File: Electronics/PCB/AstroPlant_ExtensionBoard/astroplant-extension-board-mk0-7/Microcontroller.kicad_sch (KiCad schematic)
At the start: 40 parts, among them J12 CONUFL001-SMD-T, J6 629105136821, SW3 SW_Push, U1 USBLC6-2SC6, U2 STM32WB55RGVx

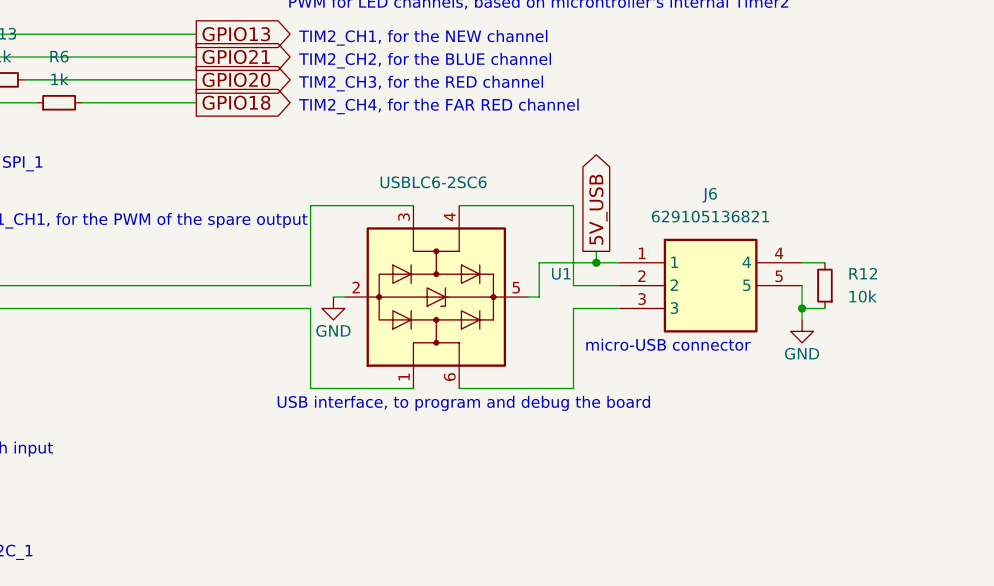
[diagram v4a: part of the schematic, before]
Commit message: Solved processing notes from aisler by changing micro usb connector
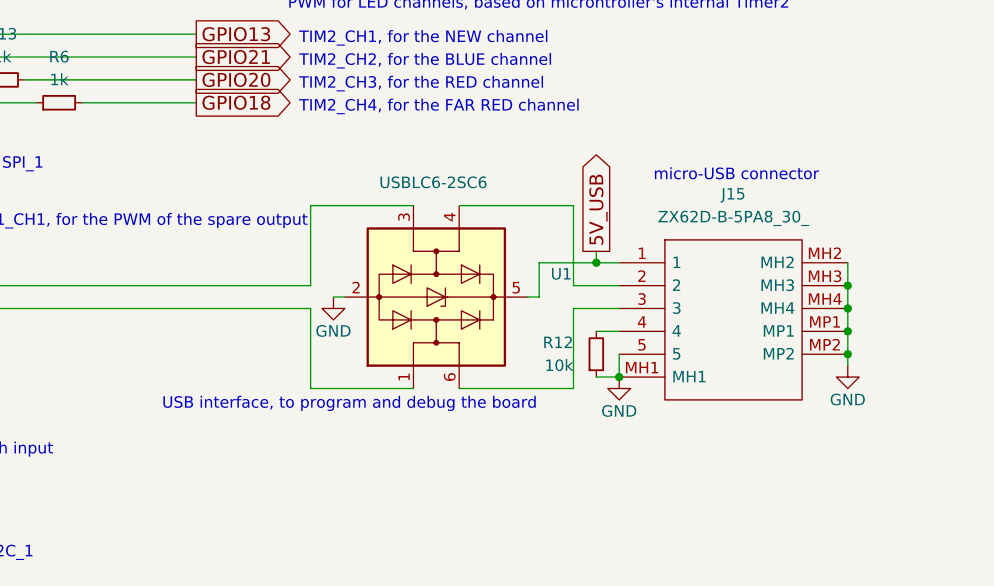
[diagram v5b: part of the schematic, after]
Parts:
- removed J6: 629105136821, SamacSys_Parts:MICRO-USB_2.0-SMT-TYPE-B_, symbol SamacSys_Parts:629105136821
- added J15: ZX62D-B-5PA8_30_, ZX62DB5PA830, symbol SamacSys_Parts:ZX62D-B-5PA8_30_
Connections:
- net 5V_USB: now also J15.1
- net GND: now also J15.5, J15.MH1, J15.MH2, J15.MH3, J15.MH4, J15.MP1, J15.MP2
- net at U1.4 (I/O2): now also J15.2
- net at U1.6 (I/O1): now also J15.3
- net at R12.2: now also J15.4
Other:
- moved on the sheet: R12

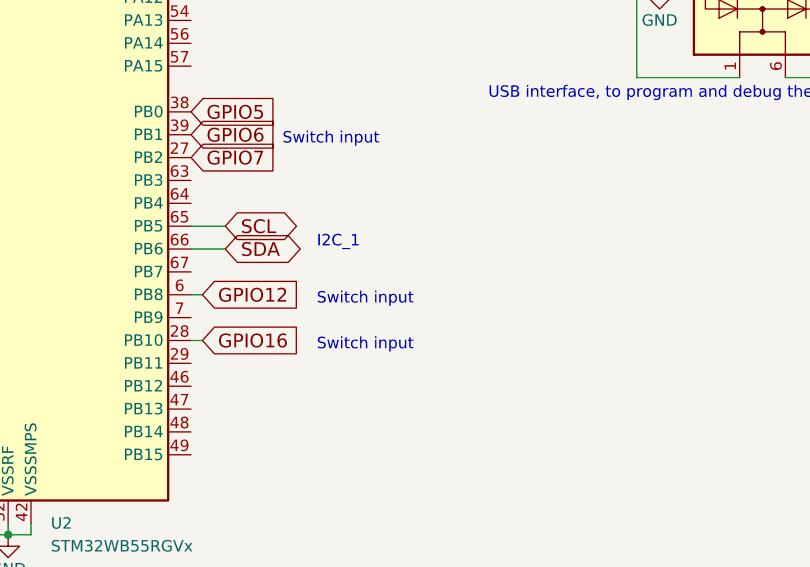
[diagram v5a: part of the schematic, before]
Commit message: Changed PCB, add a LED to simplify tests
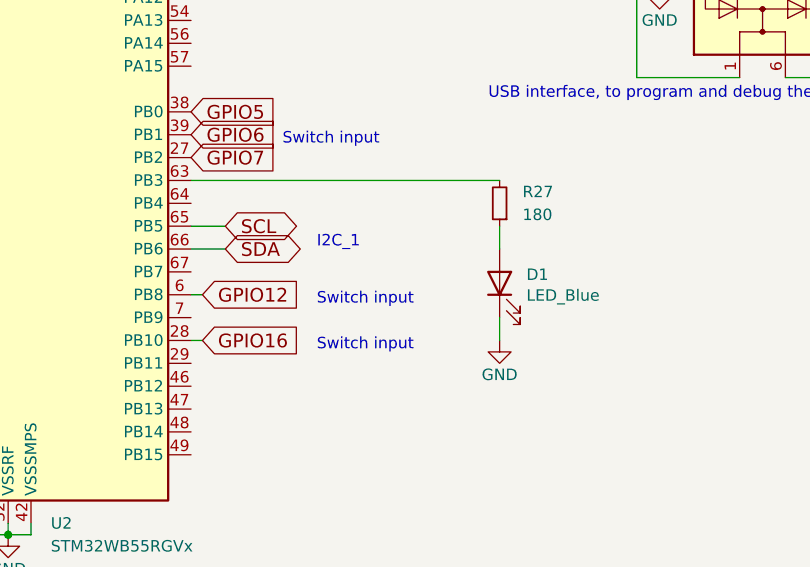
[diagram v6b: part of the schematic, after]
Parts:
- added D1: LED_Blue, LED_SMD:LED_0603_1608Metric, symbol Device:LED
- added R27: 180, Resistor_SMD:R_0603_1608Metric, symbol Device:R_Small
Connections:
- net GND: now also D1.1 (K)
- net at U2.63 (PB3): now also R27.2
- new net: D1.2 (A), R27.1
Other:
- title: (none) -> Microcontroller
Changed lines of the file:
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@@
 (kicad_sch (version 20230121) (generator eeschema)
   (paper "A4")
+  (title_block
+    (title "Microcontroller")
+    (date "2023-10-13")
+    (rev "0.7")
+    (comment 1 "Aurélien Lesage")
+  )
   (junction (at 106.68 25.4) (diameter 0) (color 0 0 0 0)
   )
@@
     (stroke (width 0) (type default))
   )
+  (wire (pts (xy 207.01 106.68) (xy 207.01 109.22))
+    (stroke (width 0) (type default))
+  )
   (wire (pts (xy 127 25.4) (xy 137.16 25.4))
     (stroke (width 0) (type default))
@@
     (stroke (width 0) (type default))
   )
+  (wire (pts (xy 172.72 101.6) (xy 207.01 101.6))
+    (stroke (width 0) (type default))
+  )
   (wire (pts (xy 105.41 124.46) (xy 113.03 124.46))
     (stroke (width 0) (type default))
@@
   )
   (wire (pts (xy 190.5 55.88) (xy 209.55 55.88))
+    (stroke (width 0) (type default))
+  )
+  (wire (pts (xy 207.01 119.38) (xy 207.01 116.84))
     (stroke (width 0) (type default))
   )
@@
     )
   )
+  (symbol (lib_id "Device:LED") (at 207.01 113.03 90) (unit 1)
+    (in_bom yes) (on_board yes) (dnp no)
+    (property "Reference" "D1" (at 209.9818 112.0648 90)
+      (effects (font (size 1.27 1.27)) (justify right))
+    )
+    (property "Value" "LED_Blue" (at 209.9818 114.3762 90)
+      (effects (font (size 1.27 1.27)) (justify right))
+    )
+    (property "Footprint" "LED_SMD:LED_0603_1608Metric" (at 207.01 113.03 0)
+      (effects (font (size 1.27 1.27)) hide)
+    )
+    (property "Datasheet" "https://fscdn.rohm.com/en/products/databook/datasheet/opto/led/chip_mono/smlen3bc8tt86-e.pdf" (at 207.01 113.03 0)
+      (effects (font (size 1.27 1.27)) hide)
+    )
+    (property "MPN" "SMLEN3BC8TT86" (at 207.01 113.03 0)
+      (effects (font (size 1.27 1.27)) hide)
+    )
+    (property "Mouser PN" " 755-SMLEN3BC8TT86 " (at 207.01 113.03 0)
+      (effects (font (size 1.27 1.27)) hide)
+    )
+    (pin "1")
+    (pin "2")
+    (instances
+      (project "Astroplant_VFR"
+        (path "/4e818498-015c-45b7-982b-80c19490efdc"
+          (reference "D1") (unit 1)
+        )
+      )
+      (project "Astroplant_AL"
+        (path "/51acab52-3cd6-4bba-9dee-c12efd332038"
+          (reference "D6") (unit 1)
+        )
+        (path "/51acab52-3cd6-4bba-9dee-c12efd332038/5f0c961f-7fa6-4a15-8a74-755a432cc19e"
+          (reference "D6") (unit 1)
+        )
+      )
+    )
+  )
   (symbol (lib_id "Device:C_Small") (at 127 27.94 0) (unit 1)
     (in_bom yes) (on_board yes) (dnp no) (fields_autoplaced)
@@
         (path "/51acab52-3cd6-4bba-9dee-c12efd332038/5f0c961f-7fa6-4a15-8a74-755a432cc19e"
           (reference "#PWR020") (unit 1)
+        )
+      )
+    )
+  )
+  (symbol (lib_id "Device:R_Small") (at 207.01 104.14 180) (unit 1)
+    (in_bom yes) (on_board yes) (dnp no) (fields_autoplaced)
+    (property "Reference" "R27" (at 209.55 102.87 0)
+      (effects (font (size 1.27 1.27)) (justify right))
+    )
+    (property "Value" "180" (at 209.55 105.41 0)
+      (effects (font (size 1.27 1.27)) (justify right))
+    )
+    (property "Footprint" "Resistor_SMD:R_0603_1608Metric" (at 207.01 104.14 0)
+      (effects (font (size 1.27 1.27)) hide)
+    )
+    (property "Datasheet" "~" (at 207.01 104.14 0)
+      (effects (font (size 1.27 1.27)) hide)
+    )
+    (property "MPN" "CRCW0603180RFKEA" (at 207.01 104.14 0)
+      (effects (font (size 1.27 1.27)) hide)
+    )
+    (pin "1")
+    (pin "2")
+    (instances
+      (project "Astroplant_AL"
+        (path "/51acab52-3cd6-4bba-9dee-c12efd332038/5f0c961f-7fa6-4a15-8a74-755a432cc19e"
+          (reference "R27") (unit 1)
+        )
+        (path "/51acab52-3cd6-4bba-9dee-c12efd332038/00000000-0000-0000-0000-00005a8053d4"
+          (reference "R11") (unit 1)
+        )
+        (path "/51acab52-3cd6-4bba-9dee-c12efd332038"
+          (reference "R27") (unit 1)
         )
       )
@@
         )
       )
+    )
+  )
+  (symbol (lib_id "power:GND") (at 207.01 119.38 0) (unit 1)
+    (in_bom yes) (on_board yes) (dnp no)
+    (property "Reference" "#PWR0127" (at 207.01 125.73 0)
+      (effects (font (size 1.27 1.27)) hide)
+    )
+    (property "Value" "GND" (at 207.01 123.19 0)
+      (effects (font (size 1.27 1.27)))
+    )
+    (property "Footprint" "" (at 207.01 119.38 0)
+      (effects (font (size 1.27 1.27)) hide)
+    )
+    (property "Datasheet" "" (at 207.01 119.38 0)
+      (effects (font (size 1.27 1.27)) hide)
+    )
+    (pin "1")
+    (instances
+      (project "Astroplant_VFR"
+        (path "/4e818498-015c-45b7-982b-80c19490efdc"
+          (reference "#PWR0127") (unit 1)
+        )
+      )
+      (project "Astroplant_AL"
+        (path "/51acab52-3cd6-4bba-9dee-c12efd332038"
+          (reference "#PWR04") (unit 1)
+        )
+        (path "/51acab52-3cd6-4bba-9dee-c12efd332038/5f0c961f-7fa6-4a15-8a74-755a432cc19e"
+          (reference "#PWR04") (unit 1)
+        )
+      )

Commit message: Updated PCB from a backup save to solve issue with git
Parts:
- removed FL1: LFB182G45CGFD436, SamacSys_Parts:LFB182G45CGFD436, symbol SamacSys_Parts:LFB182G45CGFD436
- added FL1: DEA162450BT-1260B2, DEA162450BT1295A1, symbol SamacSys_Parts:DEA162450BT-1260B2
- C10, C11, C12, C14, C5, C9: value 100nF -> VJ0603Y104MXJCW1BC
- C13: value 100pF -> VJ0603Y101KXQPW1BC
- C19, C20, C21: value 1.2pF 50V -> GRM1555C1H1R2WA01D
- C7: value 0.3pF 50VDC -> GRM1555C1HR30WA01D
- C8: value 0.8pF 50VDC -> GRM1555C1HR80BA01D
- D1: value LED_Blue -> SMLEN3BC8TT86
- R12, R24: value 10k -> CRCW060310K0DHEAP
- R13, R14, R15, R16, R17, R18, R19, R20, R21, R22, R23, R6: value 1k -> CRCW06031K00DHEBP
- R25, R26: value 0 -> CRCW04020000Z0EDC
- R27: value 180 -> CRCW0603180RFKEA
- SW3: value SW_Push -> 430156043726
- U2: value STM32WB55RGVx -> STM32WB55RGV6; MPN STM32WB55RGVx -> STM32WB55RGV6
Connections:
- net GND: now also FL1.2 (GND), FL1.4 (GND)
- net at R25.1, R26.1: now also FL1.1 (IN)
- net at C7.1, L2.2: now also FL1.3 (OUT)
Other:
- moved on the sheet: AE1, C19, C20, C21, C6, J12, L1, L3, R25, R26

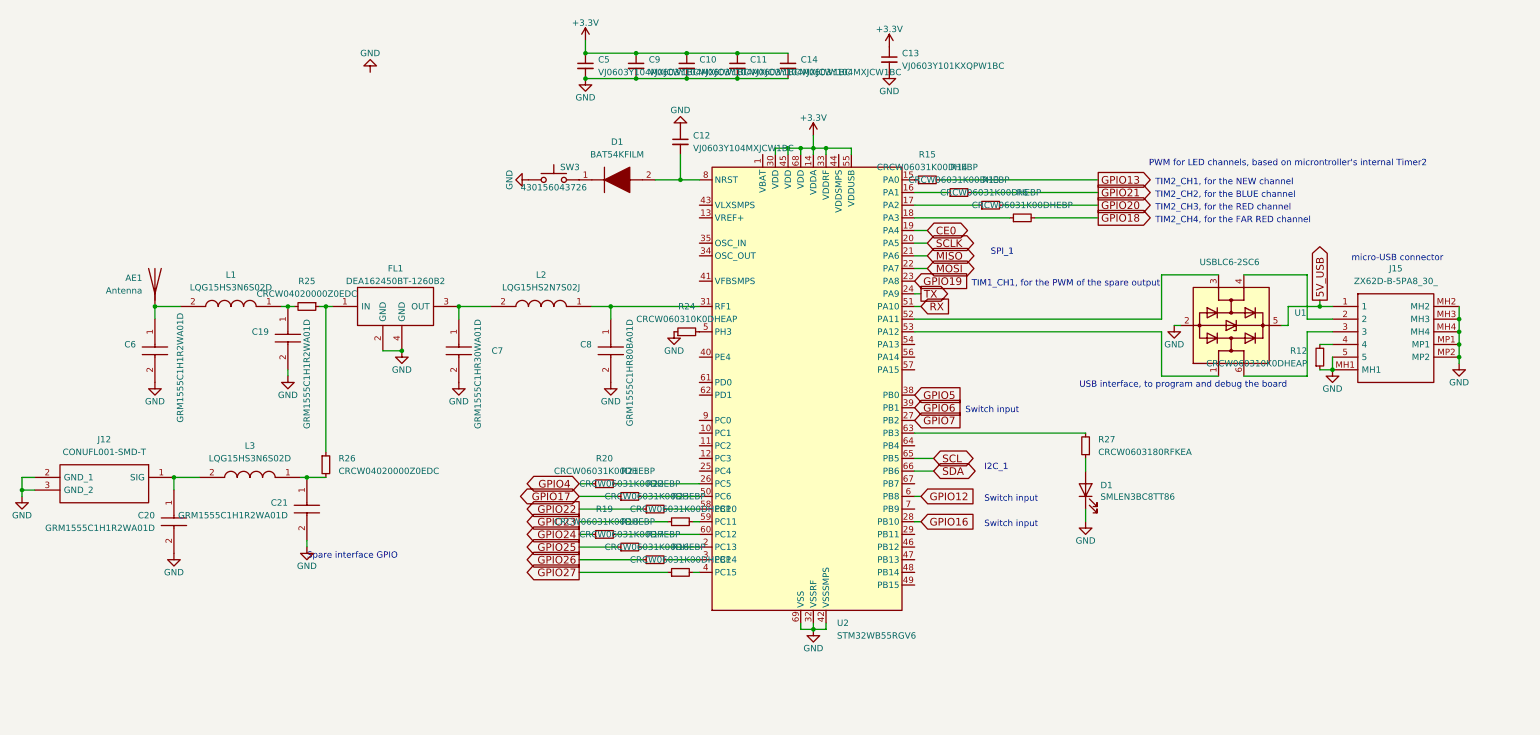
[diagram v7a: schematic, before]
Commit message: Last commit (software + hardware change)
hardware : updated readme, change pcb to solve the issues of the 1st prototype
software : add code (to create a zigbee network)
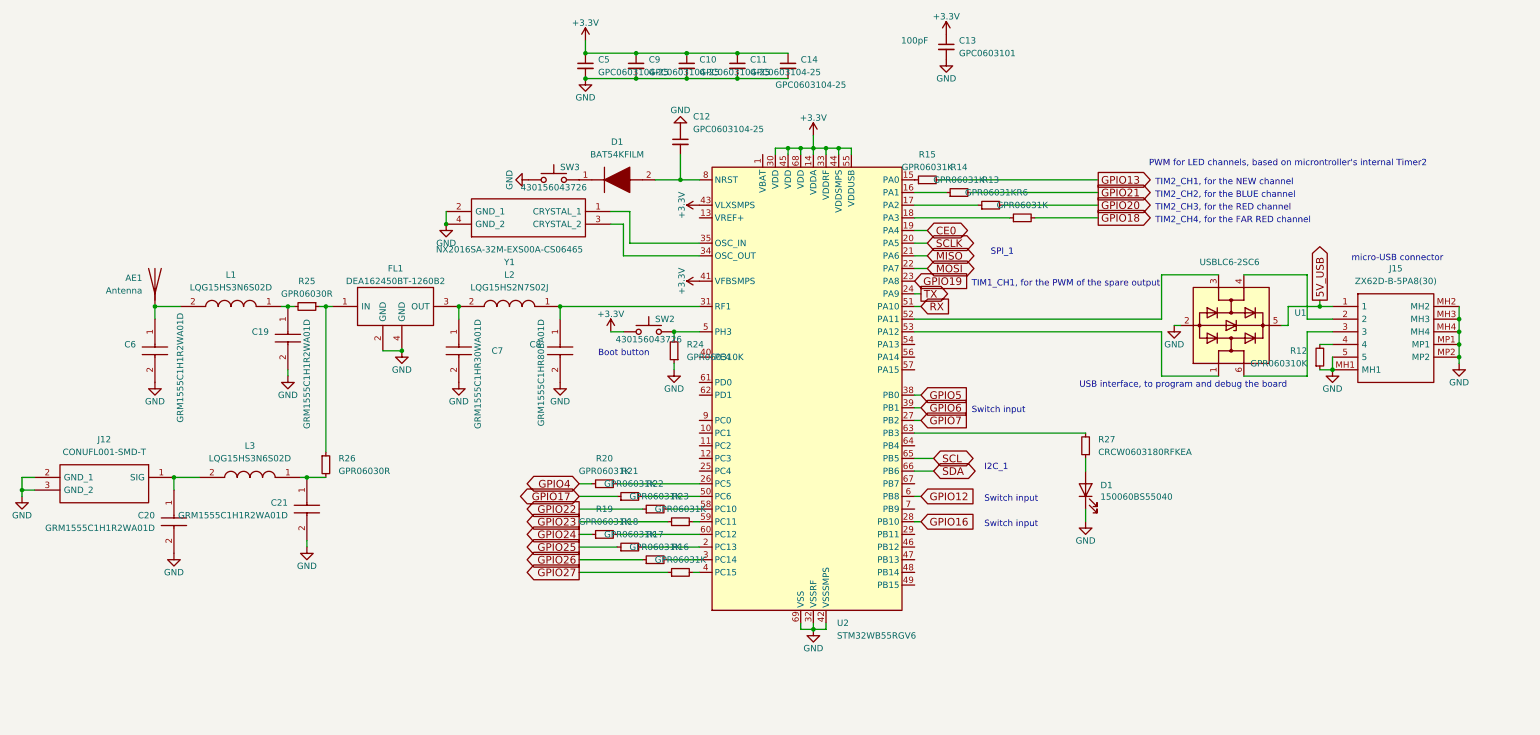
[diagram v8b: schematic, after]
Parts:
- added SW2: 430156043726, Button_Switch_THT:SW_PUSH_6mm, symbol Astroplant_VFR-rescue:SW_Push-Astroplant_VFR-rescue-Astroplant_VFR-rescue
- added Y1: NX2016SA-32M-EXS00A-CS06465, NX2016SA32MEXS00ACS06465, symbol SamacSys_Parts:NX2016SA-32M-EXS00A-CS06465
- C10, C11, C12, C14, C5, C9: value VJ0603Y104MXJCW1BC -> GPC0603104-25; Capacitance (none) -> 100nF; MPN VJ0603Y104MXJCW1BC -> GPC0603104-25
- C13: value VJ0603Y101KXQPW1BC -> GPC0603101; Capacitance (none) -> 100pF; MPN VJ0603Y101KXQPW1BC -> GPC0603101; Manufacturer_Part_Number (none) -> GPC0603101
- C19, C20, C21, C6: Capacitance (none) -> 0.8pF
- C7: Capacitance (none) -> 0.3pF
- C8: Capacitance (none) -> 1.2pF
- D1: value SMLEN3BC8TT86 -> 150060BS55040; MPN SMLEN3BC8TT86 -> 150060BS55040; Manufacturer_Part_Number (none) -> 150060BS55040
- FL1: MPN (none) -> DEA162450BT-1260B2
- J15: value ZX62D-B-5PA8_30_ -> ZX62D-B-5PA8(30); MPN (none) -> ZX62D-B-5PA8(30)
- R12, R24: value CRCW060310K0DHEAP -> GPR060310K; MPN CRCW060310K0DHEAP -> GPR060310K
- R13, R14, R15, R16, R17, R18, R19, R20, R21, R22, R23, R6: value CRCW06031K00DHEBP -> GPR06031K; MPN CRCW06031K00DHEBP -> GPR06031K
- R25, R26: value CRCW04020000Z0EDC -> GPR06030R; MPN CRCW04020000Z0EDC -> GPR06030R
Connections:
- net +3V3: now also U2.41 (VFBSMPS), U2.43 (VLXSMPS), U2.44 (VDDSMPS), SW2.1
- net GND: now also Y1.2 (GND_1), Y1.4 (GND_2)
- net at R24.2, U2.5 (PH3): now also SW2.2
- net at U2.34 (OSC_OUT): now also Y1.3 (CRYSTAL_2)
- net at U2.35 (OSC_IN): now also Y1.1 (CRYSTAL_1)
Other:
- note added: "Boot button"
- note removed: "Spare interface GPIO"
- moved on the sheet: C13, C8, L2, R24
